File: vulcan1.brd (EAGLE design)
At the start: 127 x 64.8 mm, 56 parts, among them Q1 IRF540, Q2 IRF540, T1 2N3904, T2 2N3904

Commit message: labels cleaned up
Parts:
- removed U$10: HC/49US(AT49), vulcan-1:HC/49US
- added U$8: 1X2BIG, vulcan-1:1X2BIG
- C10: value 18pf -> .1u
- C12: value .1u -> 1u; device adafruit:C025-030X050 -> adafruit:E2,5-6E
- C13, C8: value 10pf -> .1u
- C15: value 4700uf -> .1u; device adafruit:E5-13 -> adafruit:C025-030X050
- C16: value .1u -> 4700uf; device adafruit:C025-030X050 -> adafruit:E5-13
- C19: value 1u -> .1u; device adafruit:E2,5-6E -> adafruit:C025-030X050
- C20, C22: value .1u -> 10pf
- C3: value .1u -> 18pf
- C4: value 4.7u -> 18pf; device adafruit:E2,5-6E -> adafruit:C025-030X050
- C9: value 18pf -> 4.7u; device adafruit:C025-030X050 -> adafruit:E2,5-6E
- JP1: value M025MM -> (none); device SparkFun-Connectors:SCREWTERMINAL-5MM-2 -> adafruit:1X08-CLEANBIG
- JP2: value (none) -> M025MM; device adafruit:1X08-CLEANBIG -> SparkFun-Connectors:SCREWTERMINAL-5MM-2
- R1: value 560k -> 10k
- R2, R4: value 100k -> 560k
- R3: value 560k -> 100k
- R5: value 10k -> 100k
- U$1: value STM32F103XX-48PIN -> SMA; device vulcan-1:LQFP48 -> vulcan-1:SMA
- U$2: value 2X3 -> HC/49US(AT49); device vulcan-1:2X3 -> vulcan-1:HC/49US
- U$3: value 1X2BIG -> STM32F103XX-48PIN; device vulcan-1:1X2BIG -> vulcan-1:LQFP48
- U$4: value 1X2BIG -> ECX-306X; device vulcan-1:1X2BIG -> vulcan-1:ECX-306X
- U$7: value SMA -> 2X3; device vulcan-1:SMA -> vulcan-1:2X3
- U$9: value ECX-306X -> 1X2BIG; device vulcan-1:ECX-306X -> vulcan-1:1X2BIG
- moved U$7 114.7 mm to (121.9, 50.8), turned to 270 degrees
- moved C17 97.7 mm to (107.2, 39.1), turned to 90 degrees
- moved R5 90.7 mm to (103.4, 62.2), turned to 0 degrees
- moved R1 88.4 mm to (15.0, 41.9)
- moved U$2 87.7 mm to (34.3, 48.3), turned to 90 degrees
- moved C16 85.8 mm to (100.3, 10.2), turned to 270 degrees
- moved U$3 79.8 mm to (45.7, 41.9), turned to 0 degrees
- moved C21 76.8 mm to (110.7, 54.4)
- moved U$4 74.1 mm to (49.5, 19.1), turned to 180 degrees
- moved U$9 73.8 mm to (123.2, 22.9), turned to 90 degrees
- moved C6 67.9 mm to (41.9, 20.3), turned to 270 degrees
- moved C7 66.1 mm to (45.7, 50.8), turned to 0 degrees
- moved C8 64.2 mm to (47.8, 33.3), turned to 180 degrees
- moved JP1 63.7 mm to (59.7, 43.2)
- moved JP2 63.7 mm to (123.2, 38.1)
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- renumbered BMP183 to BMP1, DS1347 to DS1
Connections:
- net 3.3A: now also C10.1, C11.1, C6.1, C7.1, C8.1, C9.+, JP1.8, R2.2, U$3.24, U$3.36, U$3.48, U$7.1, U$7.2; no longer C1.1, C2.1, C20.1, C21.1, C3.1, C4.+, JP2.8, R1.2, U$1.24, U$1.36, U$1.48, U$2.1, U$2.2
- net 3.3B: now also C1.1, C15.1, C2.1, R4.2; no longer C16.1, C17.1, C22.1, R3.2
- net ACC-CS: now also JP1.5, U$3.29; no longer JP2.5, U$1.29
- net ACC-FLAG: now also JP1.6; no longer JP2.6
- net ACC-RST: now also JP1.4; no longer JP2.4
- net BOOT0: now also U$3.44, U$7.3; no longer U$1.44, U$2.3
- net BOOT1: now also U$3.20, U$7.4; no longer U$1.20, U$2.4
- net EMATCH1: now also T2.2; no longer T1.2
- net EMATCH2: now also T1.2; no longer T2.2
- net GND: now also C12.-, C15.2, C16.-, C19.2, C4.2, C9.-, JP1.7, JP2.1, R3.1, R5.1, U$1.1, U$1.2, U$3.23, U$3.35, U$3.47, U$3.9, U$7.5, U$7.6; no longer C12.2, C15.-, C16.2, C19.-, C4.-, C9.2, JP1.1, JP2.7, R2.1, R4.1, U$1.23, U$1.35, U$1.47, U$1.9, U$2.5, U$2.6, U$7.1, U$7.2
- net GPS-ANT: now also U$1.3; no longer U$7.3
- net GPS-CS: now also U$3.11; no longer U$1.11
- net N$10: now also C4.1, U$2.2, U$3.5; no longer C9.1, U$1.5, U$10.2
- net N$11: now also C19.1; no longer C7.1
- net N$12: now also C12.+, C13.1; no longer C18.1, C19.+
- net N$13: now also Q2.D, U$9.2; no longer Q1.D, U$3.2
- net N$14: now also C20.1, R2.1, R3.2; no longer C8.1, R1.1, R2.2
- net N$15: now also C22.1, R4.1, R5.2; no longer C13.1, R3.1, R4.2
- net N$17: now also Q1.D, U$8.2; no longer Q2.D, U$4.2
- net N$18: now also C21.1; no longer C12.1
- net N$2: now also U$3.8; no longer U$1.8
- net N$20: now also R1.2; no longer R5.2
- net N$21: now also R1.1; no longer R5.1
- net N$3: now also U$6.P$1; no longer U$5.P$1
- net N$4: now also U$6.P$2; no longer U$5.P$2
- net N$5: now also U$5.P$1; no longer U$6.P$1
- net N$6: now also U$5.P$2; no longer U$6.P$2
- net N$7: now also U$4.1; no longer U$9.1
- net N$8: now also U$4.4; no longer U$9.4
- net N$9: now also C3.1, U$2.1, U$3.6; no longer C10.1, U$1.6, U$10.1
- net PS-CS: now also U$3.14; no longer U$1.14
- net RTC-CS: now also U$3.25; no longer U$1.25
- net SD-CS: now also U$3.28; no longer U$1.28
- net SPI-MISO: now also JP1.2, U$3.16; no longer JP2.2, U$1.16
- net SPI-MOSI: now also JP1.1, U$3.17; no longer JP2.1, U$1.17
- net SPI-SCK: now also JP1.3, U$3.15; no longer JP2.3, U$1.15
- net USART1-RX: now also U$3.31; no longer U$1.31
- net USART1-TX: now also U$3.30; no longer U$1.30
- net USART2-RX: now also U$3.13; no longer U$1.13
- net USART2-TX: now also U$3.12; no longer U$1.12
- net USART3-CTS: now also U$3.26; no longer U$1.26
- net USART3-RTS: now also U$3.27; no longer U$1.27
- net USART3-RX: now also U$3.22; no longer U$1.22
- net USART3-TX: now also U$3.21; no longer U$1.21
- net VB-CS: now also U$3.45; no longer U$1.45
- net VBAT: now also C16.+, C17.1, C18.1, JP2.2; no longer C11.1, C15.+, C6.1, JP1.2
- net VBAT-F: now also U$8.1, U$9.1; no longer U$3.1, U$4.1
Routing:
- net N$16: track 11.2 -> 12.5 mm
- net N$1: track 12.5 -> 11.2 mm
- net GND: vias 49 -> 48
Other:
- board text added: "3.3v"
- board text added: "CS"
- board text added: "FLAG"
- board text added: "GND"
- board text added: "MISO"
- board text added: "MOSI"
- board text added: "RST"
- board text added: "SCK"

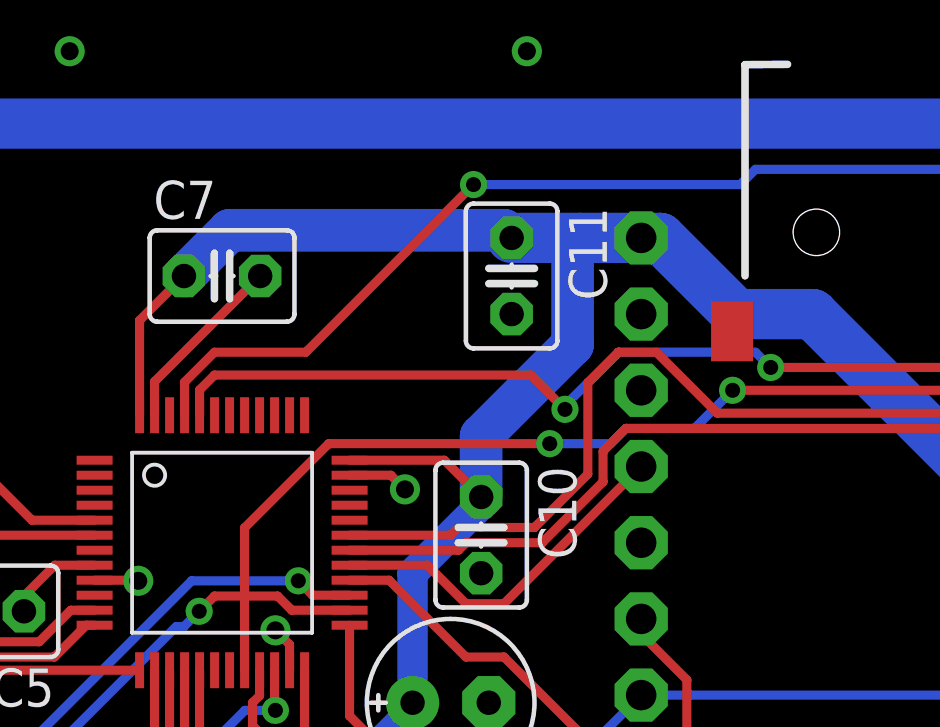
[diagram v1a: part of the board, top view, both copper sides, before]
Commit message: accelerometer reset and flag pins added
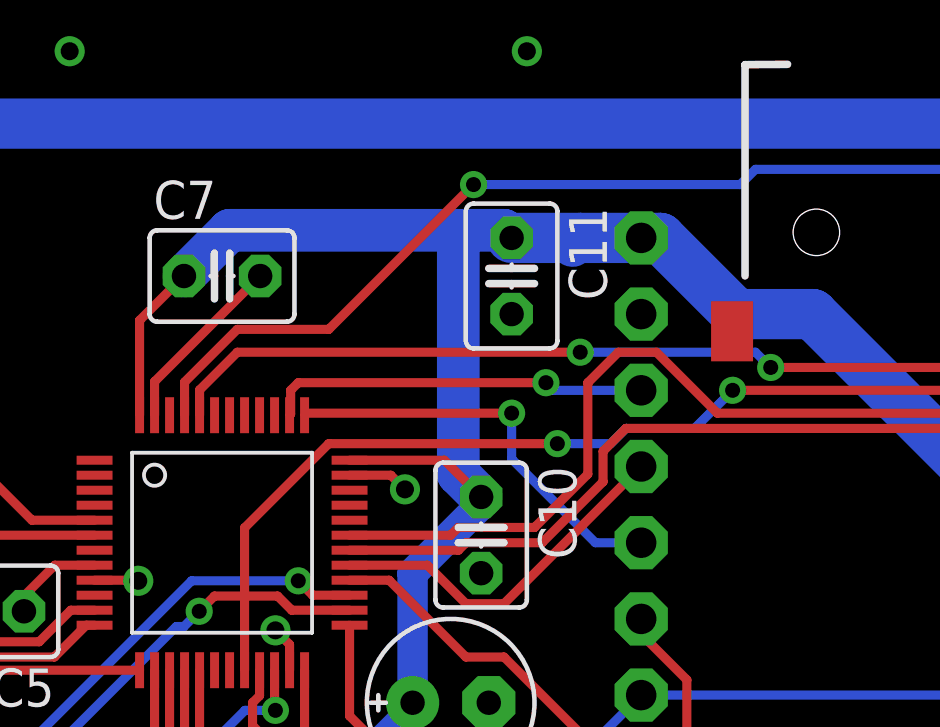
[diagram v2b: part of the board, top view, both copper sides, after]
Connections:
- net ACC-FLAG: now also U$3.38
- net ACC-RST: now also U$3.37
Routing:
- net ACC-RST: track 0.00 -> 13.9 mm, vias 0 -> 1
- net ACC-FLAG: track 0.00 -> 12.7 mm, vias 0 -> 1
- net BOOT0: track 81.8 -> 80.8 mm
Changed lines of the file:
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@@
 <element name="C10" library="adafruit" package="C025-030X050" value=".1u" x="54.356" y="42.164" smashed="yes" rot="R270">
 <attribute name="NAME" x="56.261" y="44.45" size="1.27" layer="25" font="vector" ratio="10" rot="R270"/>
-<attribute name="VALUE" x="51.308" y="44.45" size="1.27" layer="27" font="vector" ratio="10" rot="R270"/>
+<attribute name="VALUE" x="51.308" y="42.672" size="1.27" layer="27" font="vector" ratio="10" rot="R270"/>
 </element>
 <element name="C9" library="adafruit" package="E2,5-6E" value="4.7u" x="53.34" y="36.576" smashed="yes">
@@
 <wire x1="59.69" y1="52.07" x2="57.658" y2="52.07" width="1.6764" layer="16"/>
 <wire x1="57.658" y1="52.07" x2="55.372" y2="52.07" width="1.6764" layer="16"/>
-<wire x1="54.356" y1="43.434" x2="54.356" y2="45.466" width="1.4224" layer="16"/>
-<wire x1="54.356" y1="45.466" x2="57.404" y2="48.514" width="1.4224" layer="16"/>
-<wire x1="57.404" y1="48.514" x2="57.404" y2="51.816" width="1.4224" layer="16"/>
 <wire x1="57.404" y1="51.816" x2="57.658" y2="52.07" width="1.4224" layer="16"/>
 <wire x1="44.45" y1="50.8" x2="45.974" y2="52.324" width="1.4224" layer="16"/>
-<wire x1="45.974" y1="52.324" x2="55.118" y2="52.324" width="1.4224" layer="16"/>
+<wire x1="45.974" y1="52.324" x2="53.594" y2="52.324" width="1.4224" layer="16"/>
+<wire x1="53.594" y1="52.324" x2="55.118" y2="52.324" width="1.4224" layer="16"/>
 <wire x1="55.118" y1="52.324" x2="55.372" y2="52.07" width="1.4224" layer="16"/>
 <wire x1="49.97" y1="44.66" x2="53.13" y2="44.66" width="0.3048" layer="1"/>
@@
 <wire x1="92.329" y1="42.037" x2="94.742" y2="44.45" width="1.6764" layer="16"/>
 <wire x1="94.742" y1="44.45" x2="96.774" y2="44.45" width="1.6764" layer="16"/>
+<wire x1="53.594" y1="44.196" x2="53.594" y2="52.324" width="1.4224" layer="16"/>
+<wire x1="53.594" y1="44.196" x2="54.356" y2="43.434" width="1.4224" layer="16"/>
 </signal>
 <signal name="N$11">
@@
 <wire x1="105.029" y1="50.927" x2="105.156" y2="50.8" width="0.3048" layer="1"/>
 <wire x1="44.47" y1="46.16" x2="44.47" y2="47.264" width="0.3048" layer="1"/>
-<wire x1="44.47" y1="47.264" x2="45.466" y2="48.26" width="0.3048" layer="1"/>
-<wire x1="45.466" y1="48.26" x2="48.514" y2="48.26" width="0.3048" layer="1"/>
-<wire x1="48.514" y1="48.26" x2="54.102" y2="53.848" width="0.3048" layer="1"/>
+<wire x1="44.47" y1="47.264" x2="46.228" y2="49.022" width="0.3048" layer="1"/>
 <via x="54.102" y="53.848" extent="1-16" drill="0.5"/>
 <wire x1="97.028" y1="50.8" x2="105.156" y2="50.8" width="0.3048" layer="16"/>
@@
 <wire x1="84.328" y1="54.356" x2="88.392" y2="50.292" width="0.3048" layer="16"/>
 <wire x1="88.392" y1="50.292" x2="93.218" y2="50.292" width="0.3048" layer="16"/>
+<wire x1="46.228" y1="49.022" x2="49.276" y2="49.022" width="0.3048" layer="1"/>
+<wire x1="49.276" y1="49.022" x2="54.102" y2="53.848" width="0.3048" layer="1"/>
 </signal>
 <signal name="N$12">
@@
 <contactref element="U$7" pad="3"/>
 <wire x1="44.97" y1="46.16" x2="44.97" y2="47.002" width="0.3048" layer="1"/>
-<wire x1="44.97" y1="47.002" x2="45.466" y2="47.498" width="0.3048" layer="1"/>
-<wire x1="45.466" y1="47.498" x2="56.007" y2="47.498" width="0.3048" layer="1"/>
-<wire x1="56.007" y1="47.498" x2="57.15" y2="46.355" width="0.3048" layer="1"/>
-<via x="57.15" y="46.355" extent="1-16" drill="0.5"/>
-<wire x1="57.15" y1="46.355" x2="57.15" y2="46.482" width="0.3048" layer="16"/>
-<wire x1="57.15" y1="46.482" x2="58.928" y2="48.26" width="0.3048" layer="16"/>
-<wire x1="58.928" y1="48.26" x2="63.5" y2="48.26" width="0.3048" layer="16"/>
+<via x="57.658" y="48.26" extent="1-16" drill="0.5"/>
+<wire x1="57.658" y1="48.26" x2="63.5" y2="48.26" width="0.3048" layer="16"/>
 <wire x1="63.5" y1="48.26" x2="64.008" y2="47.752" width="0.3048" layer="16"/>
 <via x="64.008" y="47.752" extent="1-16" drill="0.5"/>
@@
 <wire x1="88.9" y1="54.61" x2="82.042" y2="47.752" width="0.3048" layer="1"/>
 <wire x1="82.042" y1="47.752" x2="64.008" y2="47.752" width="0.3048" layer="1"/>
+<wire x1="44.97" y1="47.002" x2="46.228" y2="48.26" width="0.3048" layer="1"/>
+<wire x1="46.228" y1="48.26" x2="57.658" y2="48.26" width="0.3048" layer="1"/>
 </signal>
 <signal name="BOOT1">
@@
 <wire x1="46.47" y1="37.66" x2="46.47" y2="42.406" width="0.3048" layer="1"/>
 <wire x1="46.47" y1="42.406" x2="49.276" y2="45.212" width="0.3048" layer="1"/>
-<wire x1="49.276" y1="45.212" x2="56.642" y2="45.212" width="0.3048" layer="1"/>
-<via x="56.642" y="45.212" extent="1-16" drill="0.5"/>
-<wire x1="56.642" y1="45.212" x2="58.674" y2="45.212" width="0.3048" layer="16"/>
+<wire x1="49.276" y1="45.212" x2="56.896" y2="45.212" width="0.3048" layer="1"/>
+<via x="56.896" y="45.212" extent="1-16" drill="0.5"/>
+<wire x1="56.896" y1="45.212" x2="58.674" y2="45.212" width="0.3048" layer="16"/>
 <wire x1="58.674" y1="45.212" x2="59.182" y2="45.72" width="0.3048" layer="16"/>
 <wire x1="59.182" y1="45.72" x2="61.468" y2="45.72" width="0.3048" layer="16"/>
@@
 <signal name="ACC-FLAG">
 <contactref element="JP1" pad="6"/>
+<via x="56.515" y="47.244" extent="1-16" drill="0.5"/>
+<contactref element="U$3" pad="38"/>
+<wire x1="47.97" y1="46.16" x2="48.006" y2="46.196" width="0.3048" layer="1"/>
+<wire x1="48.006" y1="46.196" x2="48.006" y2="46.99" width="0.3048" layer="1"/>
+<wire x1="48.006" y1="46.99" x2="48.26" y2="47.244" width="0.3048" layer="1"/>
+<wire x1="48.26" y1="47.244" x2="56.515" y2="47.244" width="0.3048" layer="1"/>
+<wire x1="56.515" y1="47.244" x2="56.769" y2="46.99" width="0.3048" layer="16"/>
+<wire x1="56.769" y1="46.99" x2="59.69" y2="46.99" width="0.3048" layer="16"/>
 </signal>
 <signal name="N$1">
@@
 <signal name="ACC-RST">
 <contactref element="JP1" pad="4"/>
+<via x="55.372" y="46.228" extent="1-16" drill="0.5"/>
+<contactref element="U$3" pad="37"/>
+<wire x1="48.47" y1="46.16" x2="48.538" y2="46.228" width="0.3048" layer="1"/>
+<wire x1="48.538" y1="46.228" x2="55.372" y2="46.228" width="0.3048" layer="1"/>
+<wire x1="55.372" y1="46.228" x2="55.372" y2="44.704" width="0.3048" layer="16"/>
+<wire x1="55.372" y1="44.704" x2="58.166" y2="41.91" width="0.3048" layer="16"/>
+<wire x1="58.166" y1="41.91" x2="59.69" y2="41.91" width="0.3048" layer="16"/>
 </signal>
 <signal name="ACC-CS">

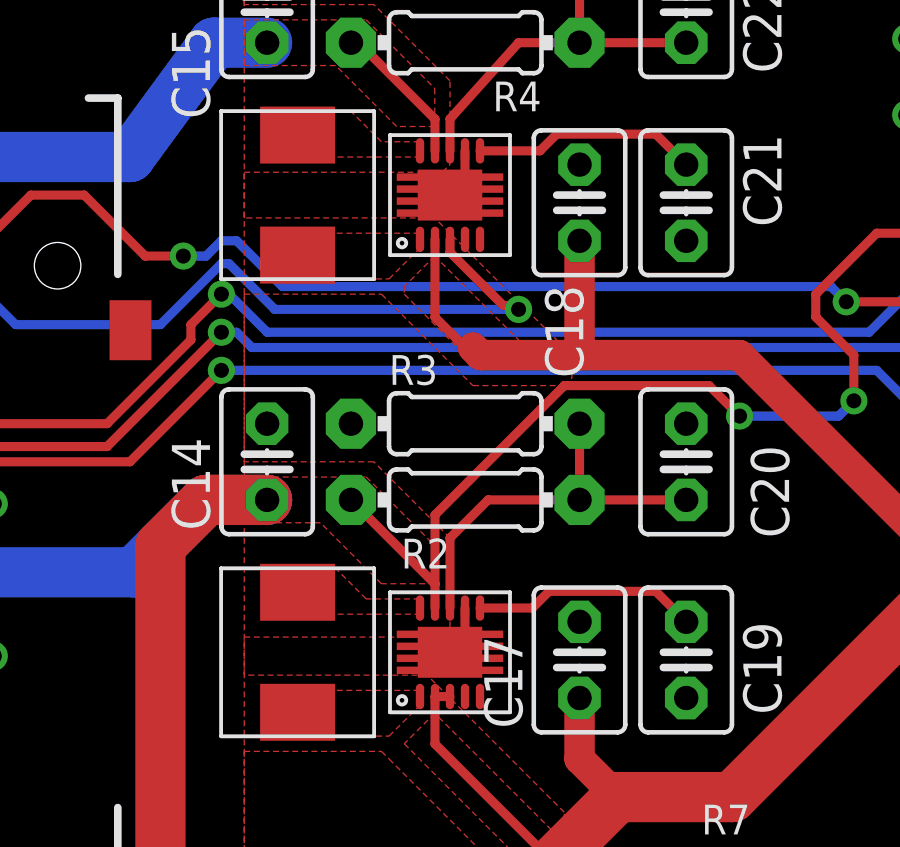
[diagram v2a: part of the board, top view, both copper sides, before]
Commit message: added gnd vias to SMPS IC's
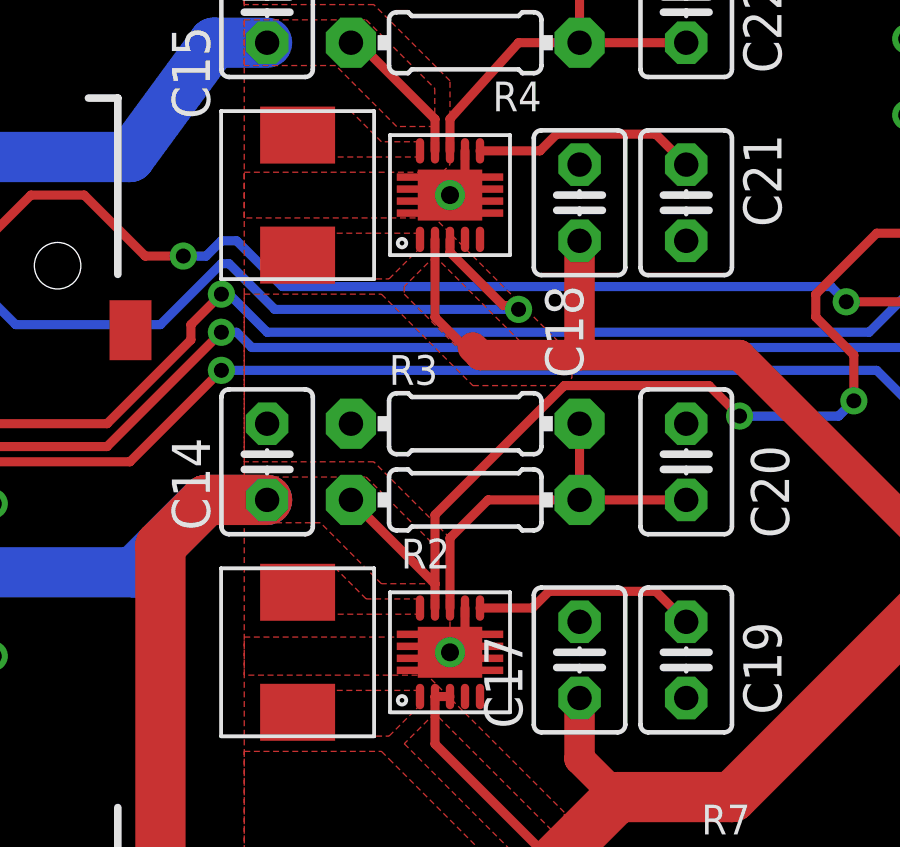
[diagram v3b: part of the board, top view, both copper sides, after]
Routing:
- net GND: vias 48 -> 50
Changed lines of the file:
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@@
 <via x="121.92" y="60.96" extent="1-16" drill="3.302" diameter="5.08"/>
 <via x="81.28" y="5.08" extent="1-16" drill="3.302" diameter="5.08"/>
+<via x="102.87" y="54.61" extent="1-16" drill="0.6"/>
+<via x="102.87" y="39.37" extent="1-16" drill="0.6"/>
 </signal>
 <signal name="N$2">

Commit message: final changes
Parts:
- removed U$9: 1X2BIG, vulcan-1:1X2BIG
- added JP4, JP5: M025MM, SparkFun-Connectors:SCREWTERMINAL-5MM-2
- U$8: value 1X2BIG -> 1X2HEADER; device vulcan-1:1X2BIG -> 1x2 header:1X2HEADER
- moved U$8 91.2 mm to (40.1, 49.0), turned to 90 degrees
- moved C14 0.25 mm to (96.5, 45.7)
- moved C7 0.25 mm to (45.7, 50.5)
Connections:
- new net N$22: U$3.39, U$8.0
- new net N$23: U$3.40, U$8.1
- net N$13: now also JP4.2; no longer U$9.2
- net N$17: now also JP5.1; no longer U$8.2
- net VBAT-F: now also JP4.1, JP5.2; no longer U$8.1, U$9.1
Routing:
- net N$22: track 0.00 -> 9.42 mm, vias 0 -> 1
- net N$23: track 0.00 -> 8.84 mm, vias 0 -> 1
- net VBAT-F: track 35.6 -> 37.6 mm
- net BOOT1: track 86.1 -> 87.1 mm
- net N$17: track 8.67 -> 7.73 mm
- net GND: track 49.9 -> 50.9 mm
- net 3.3A: track 223.2 -> 222.7 mm
